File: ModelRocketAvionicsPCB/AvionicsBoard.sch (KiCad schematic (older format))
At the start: 39 parts

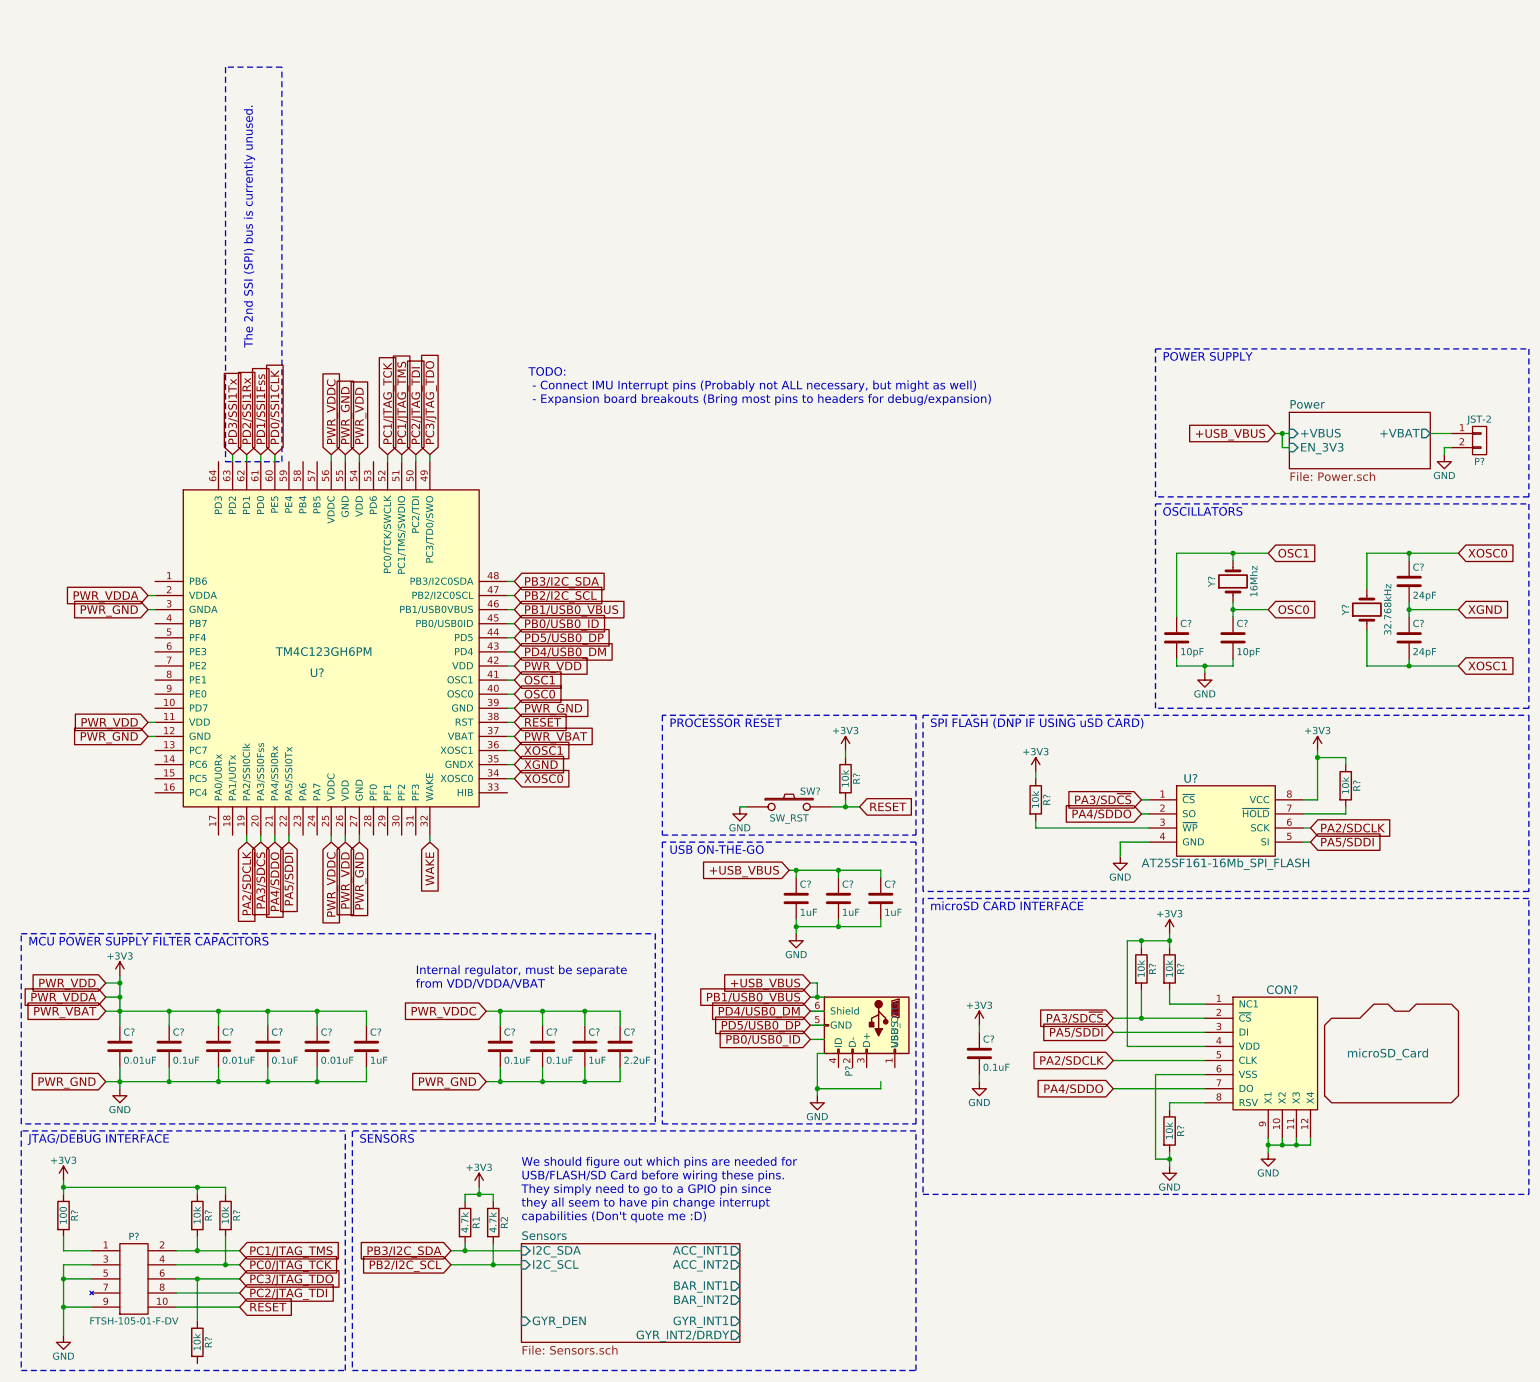
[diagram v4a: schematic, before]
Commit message: Annotated components and added 'Digi-Key Part Numbers' for most of the non-passives
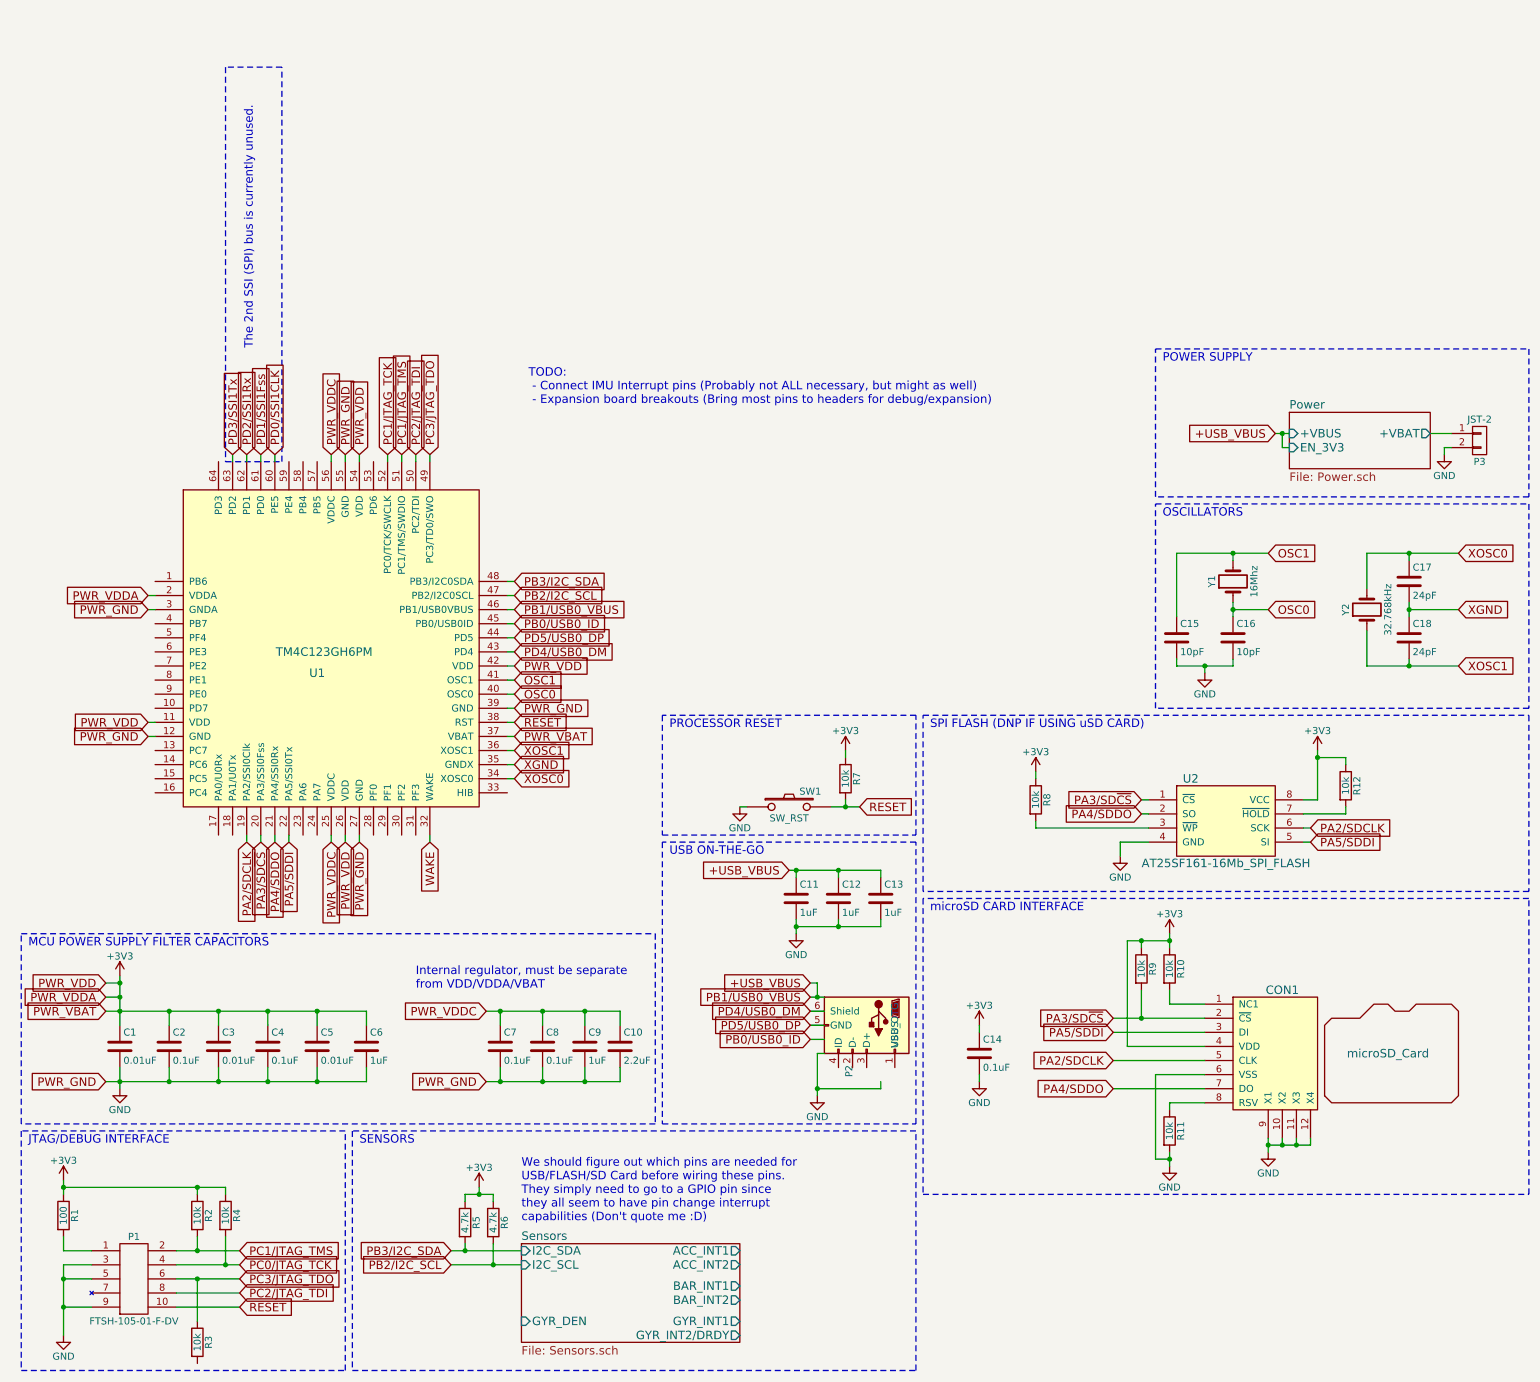
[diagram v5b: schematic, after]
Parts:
- CON1: renamed from CON?; Digi-Key Part Number (none) -> WM11190CT-ND
- P1: renamed from P?; Digi-Key Part Number (none) -> SAM9434-ND
- P2: renamed from P?; Digi-Key Part Number (none) -> 609-4053-1-ND
- U1: renamed from U?; Digi-Key Part Number (none) -> 296-46360-1-ND
- U2: renamed from U?; Digi-Key Part Number (none) -> 1265-1230-1-ND
- gave numbers to parts that had none: 32
- renumbered R1 to R5, R2 to R6

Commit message: Added pin allocation excel sheet for planning/documentation
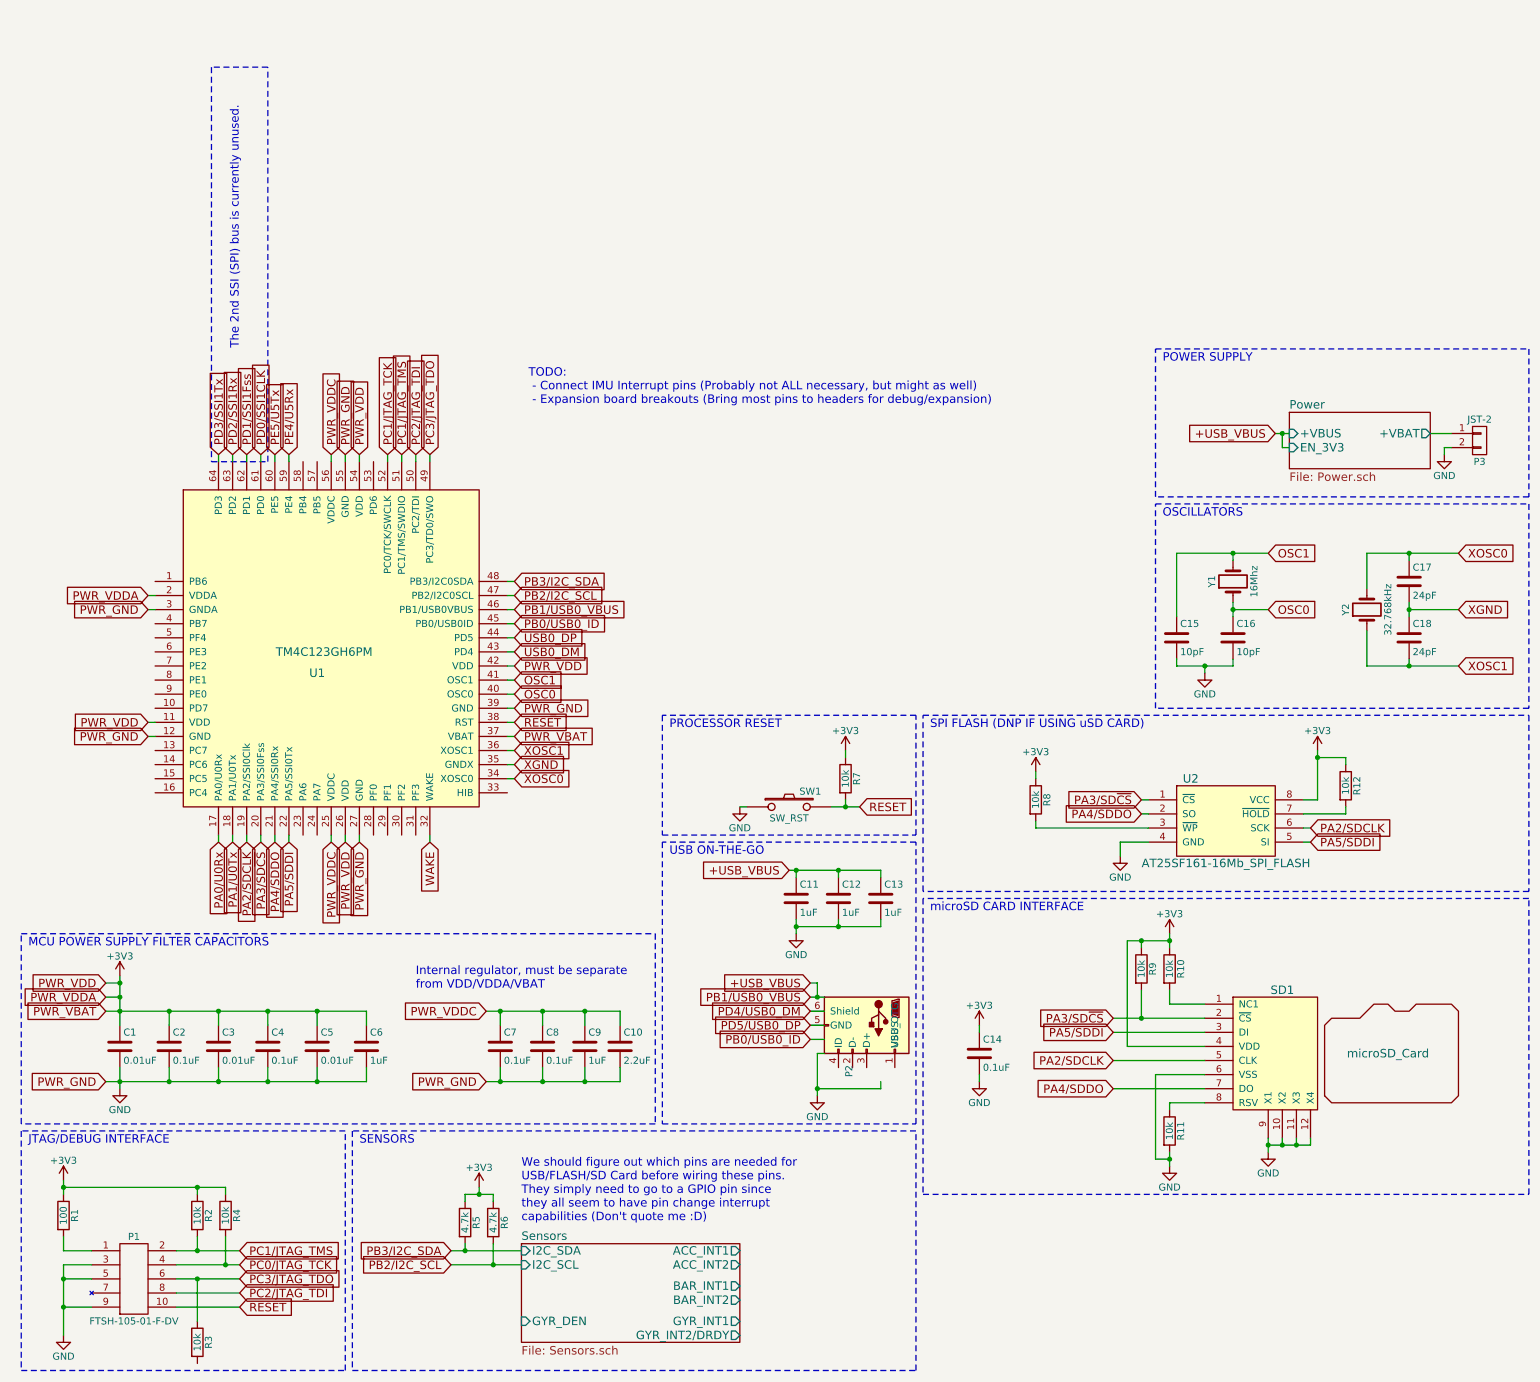
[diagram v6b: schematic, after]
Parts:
- renumbered CON1 to SD1
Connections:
- net PD0/SSI1CLK: now also U1.61 (PD0); no longer U1.60 (PE5)
- net PD1/SSI1Fss: now also U1.62 (PD1); no longer U1.61 (PD0)
- net PD2/SSI1Rx: now also U1.63 (PD2); no longer U1.62 (PD1)
- net PD3/SSI1Tx: now also U1.64 (PD3); no longer U1.63 (PD2)
- net PD4/USB0_DM: no longer U1.43 (PD4)
- net PD5/USB0_DP: no longer U1.44 (PD5)
- net PA0/U0Rx: now reaches U1.17 (PA0/U0Rx)
- net PA1/U0Tx: now reaches U1.18 (PA1/U0Tx)
- net PE4/U5Rx: now reaches U1.59 (PE4)
- new net PE5/U5Tx: U1.60 (PE5)
- new net USB0_DM: U1.43 (PD4)
- new net USB0_DP: U1.44 (PD5)
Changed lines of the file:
@@
 EESchema Schematic File Version 2
+LIBS:AvionicsBoard-rescue
 LIBS:power
 LIBS:device
@@
 $EndSheet
 Text GLabel 4000 2650 2    60   Input ~ 0
-PD4/USB0_DM
+USB0_DM
 Text GLabel 4000 2550 2    60   Input ~ 0
-PD5/USB0_DP
+USB0_DP
 Text GLabel 4000 3150 2    60   Input ~ 0
 RESET
@@
 Internal regulator, must be separate\nfrom VDD/VDDA/VBAT
 $Comp
-L microSD_Card CON1
+L microSD_Card SD1
 U 1 1 5AEA02E7
 P 9450 5500
-F 0 "CON1" H 9450 5950 60  0000 C CNN
+F 0 "SD1" H 9450 5950 60  0000 C CNN
 F 1 "microSD_Card" H 10200 5500 60  0000 C CNN
 F 2 "" H 9450 5450 60  0001 C CNN
@@
 Text GLabel 2300 4000 3    60   Input ~ 0
 PA4/SDDO
-Text GLabel 2300 1250 1    60   Input ~ 0
+Text GLabel 2200 1250 1    60   Input ~ 0
 PD0/SSI1CLK
-Text GLabel 2200 1250 1    60   Input ~ 0
+Text GLabel 2100 1250 1    60   Input ~ 0
 PD1/SSI1Fss
-Text GLabel 2100 1250 1    60   Input ~ 0
+Text GLabel 2000 1250 1    60   Input ~ 0
 PD2/SSI1Rx
-Text GLabel 2000 1250 1    60   Input ~ 0
+Text GLabel 1900 1250 1    60   Input ~ 0
 PD3/SSI1Tx
 $Comp
@@
 	2100 3950 2100 4000
 Wire Wire Line
+	1900 1250 1900 1300
+Wire Wire Line
 	2000 1250 2000 1300
 Wire Wire Line
@@
 Wire Wire Line
 	2200 1250 2200 1300
-Wire Wire Line
-	2300 1250 2300 1300
 Wire Wire Line
 	8450 3700 8500 3700
@@
 Text Notes 4100 900  0    60   ~ 0
 TODO:\n - Connect IMU Interrupt pins (Probably not ALL necessary, but might as well)\n - Expansion board breakouts (Bring most pins to headers for debug/expansion)\n
-Text Notes 2150 500  1    60   ~ 0
+Text Notes 2050 500  1    60   ~ 0
 The 2nd SSI (SPI) bus is currently unused.
 Wire Notes Line
-	1950 -1500 1950 1300
-Wire Notes Line
-	1950 1300 2350 1300
-Wire Notes Line
-	2350 1300 2350 -1500
-Wire Notes Line
-	2350 -1500 1950 -1500
+	1850 -1500 1850 1300
+Wire Notes Line
+	1850 1300 2250 1300
+Wire Notes Line
+	2250 1300 2250 -1500
+Wire Notes Line
+	2250 -1500 1850 -1500
 $Comp
 L GND #PWR16
@@
 Text Notes 8600 600  0    60   ~ 0
 POWER SUPPLY
+Text GLabel 2400 1250 1    60   Input ~ 0
+PE4/U5Rx
+Text GLabel 2300 1250 1    60   Input ~ 0
+PE5/U5Tx
+Wire Wire Line
+	2300 1250 2300 1300
+Wire Wire Line
+	2400 1250 2400 1300
+Text GLabel 1900 4000 3    60   Input ~ 0
+PA0/U0Rx
+Text GLabel 2000 4000 3    60   Input ~ 0
+PA1/U0Tx
+Wire Wire Line
+	2000 4000 2000 3950
+Wire Wire Line
+	1900 4000 1900 3950
 $EndSCHEMATC

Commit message: Added User switches and LED to the pcb schematic
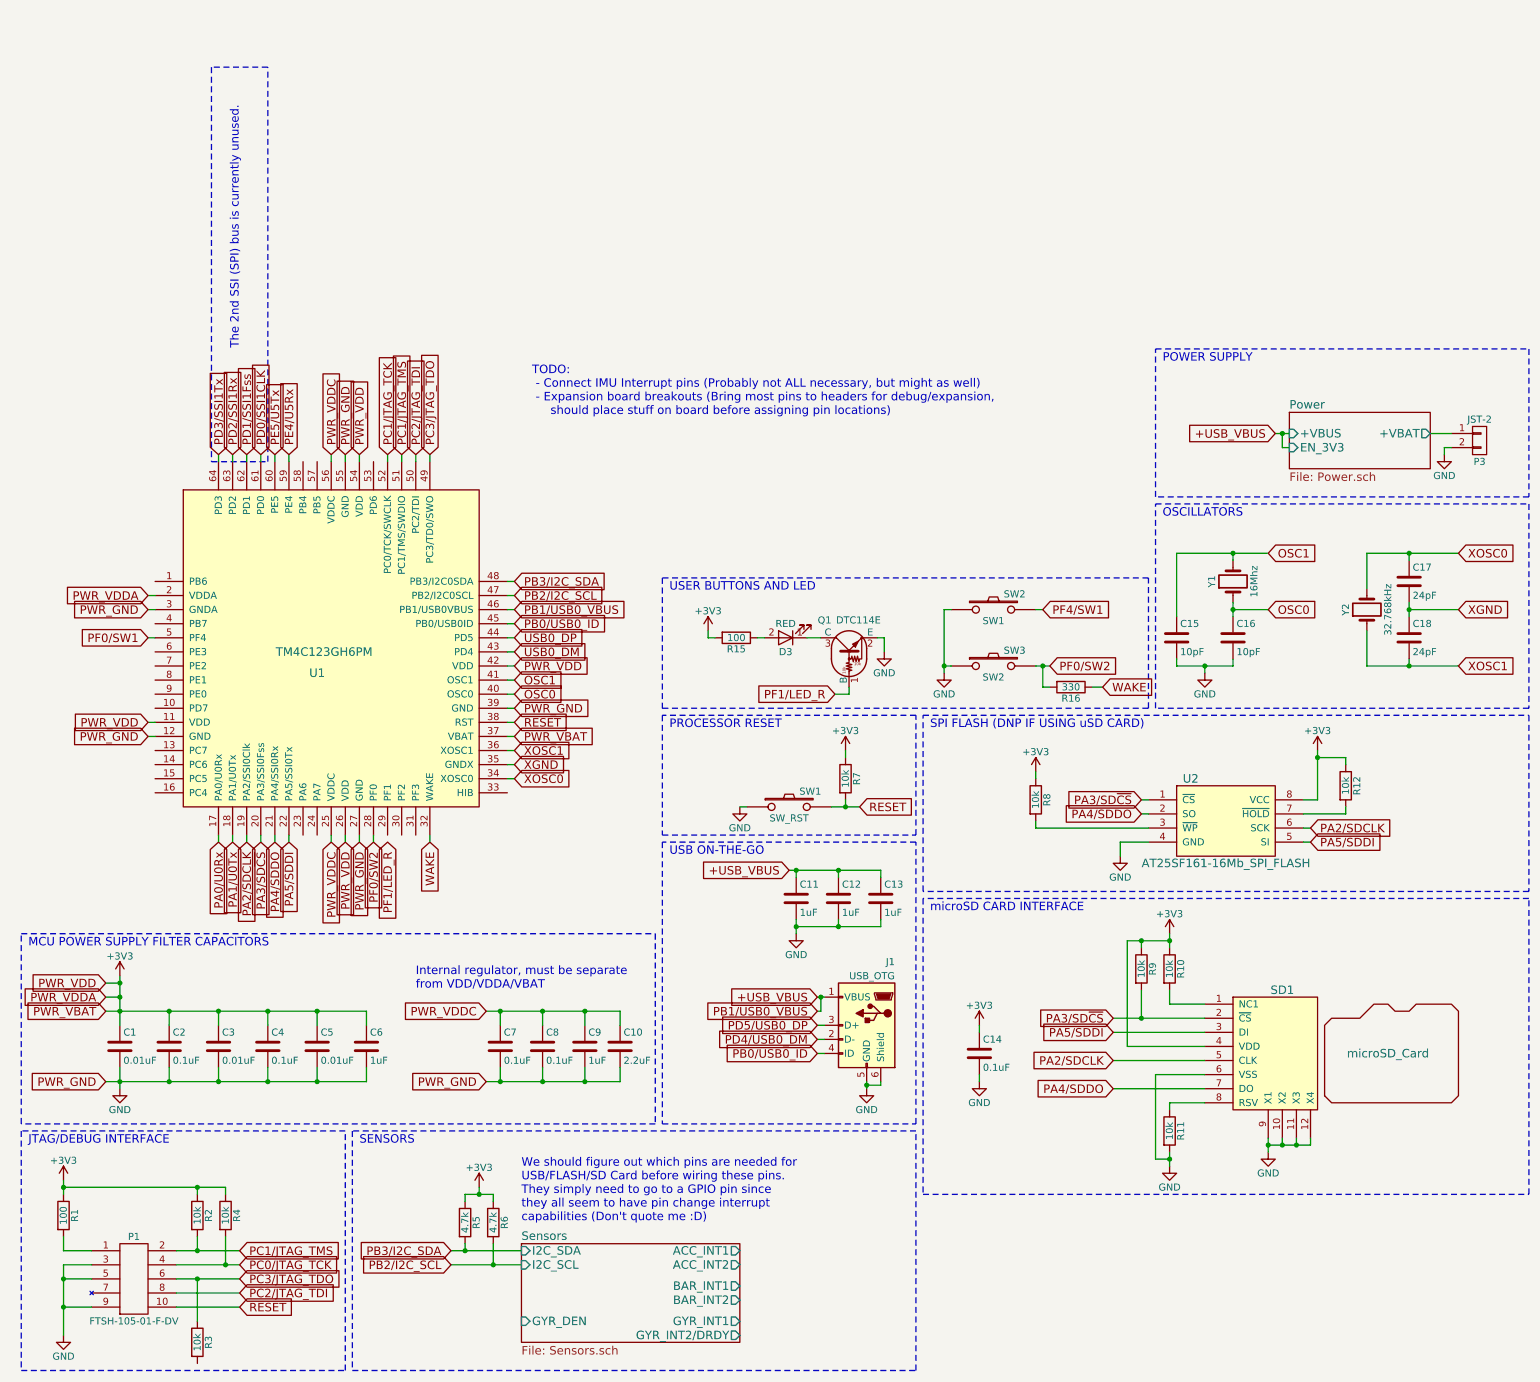
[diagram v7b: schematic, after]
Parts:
- removed P2: USB_OTG, symbol USB_OTG
- added D3: RED, symbol LED
- added J1: USB_OTG, symbol USB_OTG
- added Q1: DTC114E, symbol DTC114E
- added R15: 100, symbol R
- added R16: 330, symbol R
- added SW2: SW1, symbol SW_PUSH
- added SW3: SW2, symbol SW_PUSH
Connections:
- net +3V3: now also R15.2
- net +USB_VBUS: now also J1.1 (VBUS)
- net GND: now also J1.5 (GND), J1.6 (Shield), Q1.2 (E), SW2.1, SW3.1
- net PB0/USB0_ID: now also J1.4 (ID)
- net PD4/USB0_DM: now also J1.2 (D-)
- net PD5/USB0_DP: now also J1.3 (D+)
- net WAKE: now also R16.1
- net PF0/SW2: now reaches U1.28 (PF0)
- net PF0/SW2: now also R16.2, SW3.2
- net PF0/SW1: now reaches U1.5 (PF4)
- new net: D3.1 (K), Q1.3 (C)
- new net: D3.2 (A), R15.1
- new net PF1/LED_R: Q1.1 (B)
- new net PF4/SW1: SW2.2
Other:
- note added: "TODO:\n - Connect IMU Interrupt pins (Probably not ALL necessary, but might as well)\n - Expansion board breakouts (Bring most pins to headers for debug/expansion,\n should place stuff on board before assigning pin locations)\n\n"
- note added: "USER BUTTONS AND LED"
- note removed: "TODO:\n - Connect IMU Interrupt pins (Probably not ALL necessary, but might as well)\n - Expansion board breakouts (Bring most pins to headers for debug/expansion)\n"
